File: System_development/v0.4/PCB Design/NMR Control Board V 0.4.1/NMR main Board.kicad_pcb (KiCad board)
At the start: 2 copper layers, 139.7 x 88.9 mm, 58 parts

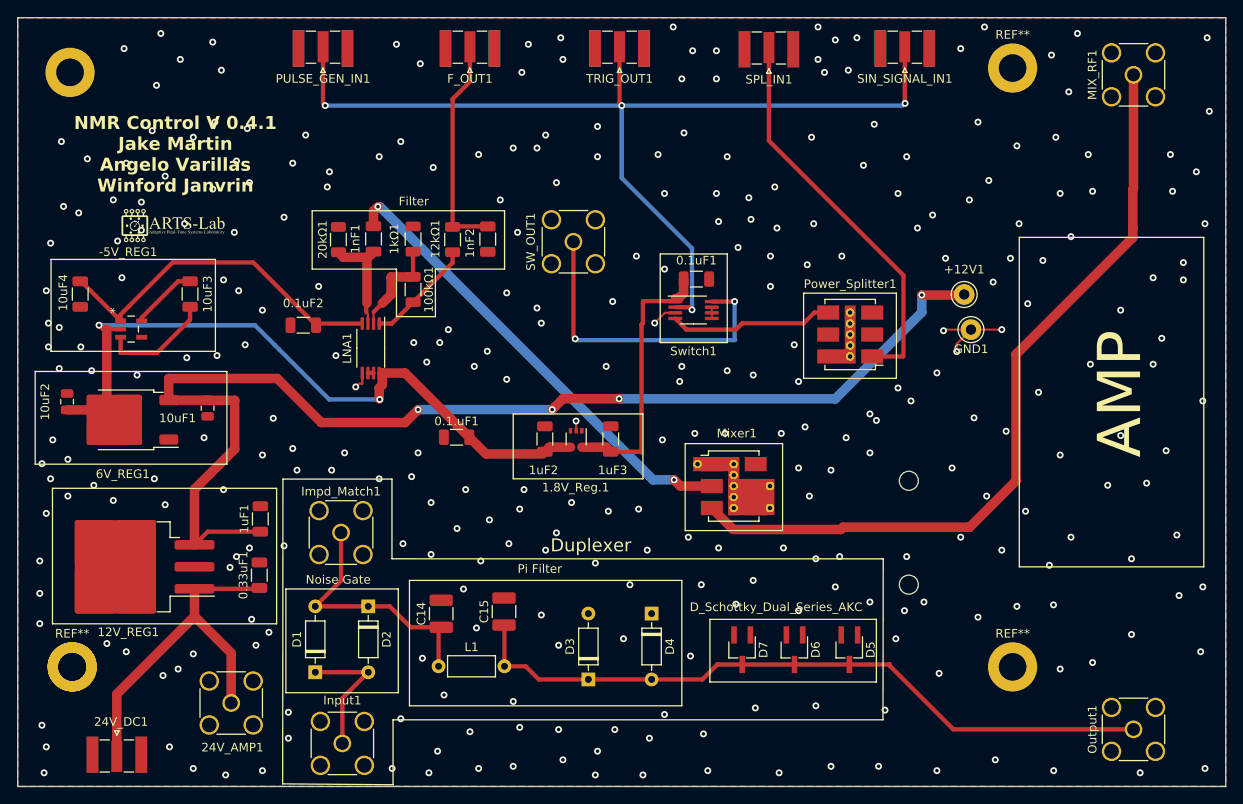
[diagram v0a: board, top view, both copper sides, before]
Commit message: Updated the NMR Board
No warning on the board, looks good order
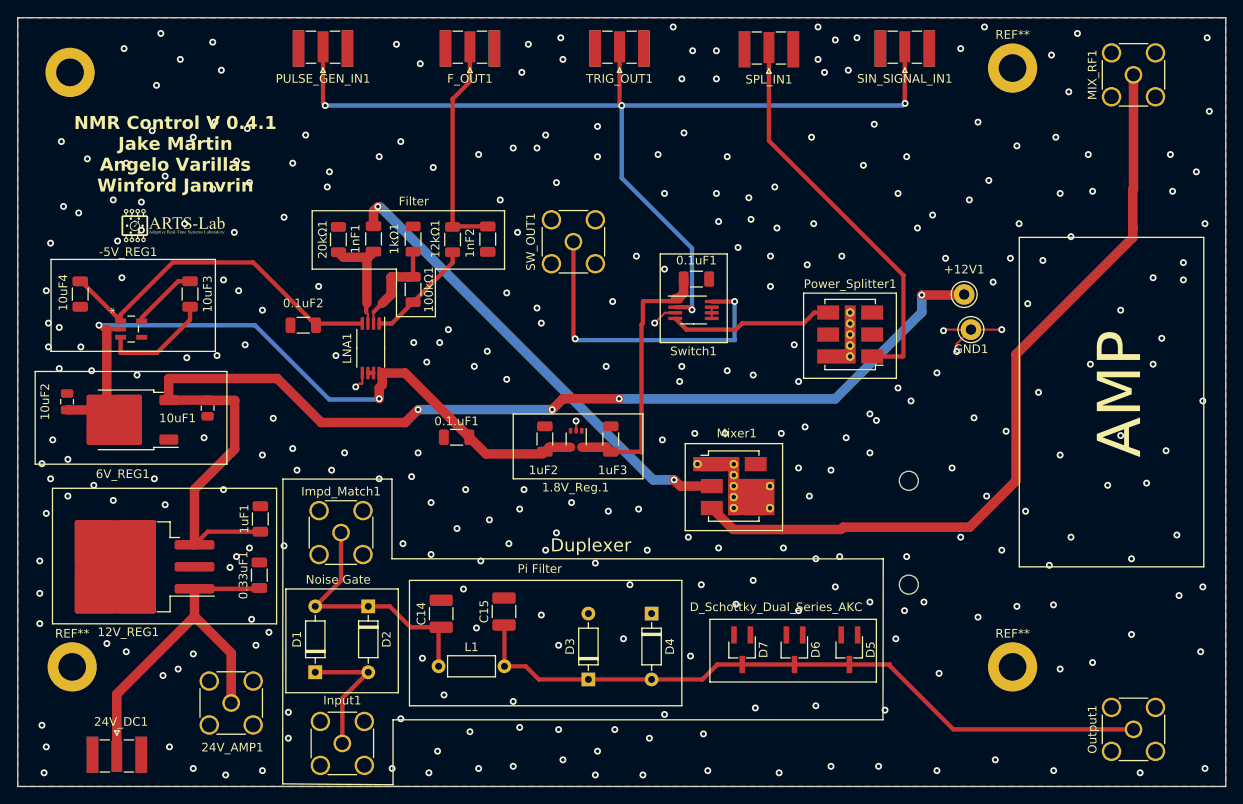
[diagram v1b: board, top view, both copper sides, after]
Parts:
- removed the REF** at (82.5, 118.2)
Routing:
- net Net-(D3-K): track 82.7 -> 82.1 mm
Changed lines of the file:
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@@
       (net 25 "Net-(-5V_REG1-C1+)") (pinfunction "C1+") (pintype "passive"))
   )
-  (footprint "MountingHole:MountingHole_3.2mm_M3_ISO7380_Pad" (layer "F.Cu")
-    (at 82.5 118.25)
-    (descr "Mounting Hole 3.2mm, M3, ISO7380")
-    (tags "mounting hole 3.2mm m3 iso7380")
-    (attr exclude_from_pos_files exclude_from_bom)
-    (fp_text reference "REF**" (at 0 -3.85) (layer "F.SilkS") hide
-        (effects (font (size 1 1) (thickness 0.15)))
-    )
-    (fp_text value "MountingHole_3.2mm_M3_ISO7380_Pad" (at 0 3.85) (layer "F.Fab")
-        (effects (font (size 1 1) (thickness 0.15)))
-    )
-    (fp_text user "${REFERENCE}" (at 0 0) (layer "F.Fab")
-        (effects (font (size 1 1) (thickness 0.15)))
-    )
-    (fp_circle (center 0 0) (end 2.85 0)
-      (stroke (width 0.15) (type solid)) (fill none) (layer "Cmts.User"))
-    (fp_circle (center 0 0) (end 3.1 0)
-      (stroke (width 0.05) (type solid)) (fill none) (layer "F.CrtYd"))
-    (pad "3" thru_hole circle (at 0 0) (size 5.7 5.7) (drill 3.2) (layers "*.Cu" "*.Mask"))
-  )
   (footprint "Connector_Coaxial:SMA_Samtec_SMA-J-P-X-ST-EM1_EdgeMount" (layer "F.Cu")
     (at 87.661 128.409)
@@
   (segment (start 159.9844 117.974) (end 166.0296 117.974) (width 0.5) (layer "F.Cu") (net 4))
   (segment (start 149.5044 119.7046) (end 155.3774 119.7046) (width 0.5) (layer "F.Cu") (net 4))
-  (segment (start 172.3644 118.3166) (end 172.3644 117.6531) (width 0.25) (layer "F.Cu") (net 4))
   (segment (start 132.4864 113.4626) (end 132.4864 118.1806) (width 0.5) (layer "F.Cu") (net 4))
   (segment (start 132.4356 113.4118) (end 132.4864 113.4626) (width 0.25) (layer "F.Cu") (net 4))
@@
   (segment (start 104.255 102.616) (end 98.165 102.616) (width 0.5) (layer "F.Cu") (net 13))
   (segment (start 93.666 84.896) (end 106.2066 84.896) (width 1.1) (layer "F.Cu") (net 13))
-  (segment (start 122.5 88.5) (end 122.5444 88.5444) (width 0.5) (layer "F.Cu") (net 13))
   (segment (start 96.641 104.14) (end 96.641 97.7198) (width 1.1) (layer "F.Cu") (net 13))
   (segment (start 122.4556 88.5444) (end 122.5 88.5) (width 0.5) (layer "F.Cu") (net 13))
-  (segment (start 122.5444 88.5444) (end 122.6058 88.5444) (width 0.5) (layer "F.Cu") (net 13))
   (segment (start 121 90) (end 122.4556 88.5444) (width 1.1) (layer "F.Cu") (net 13))
   (segment (start 139.25 87.25) (end 145.75 87.25) (width 1.1) (layer "F.Cu") (net 13))
@@
   (segment (start 87.661 121.3887) (end 87.661 128.609) (width 1.1) (layer "F.Cu") (net 21))
   (segment (start 104.042 109.22) (end 104.14 109.122) (width 0.5) (layer "F.Cu") (net 21))
-  (segment (start 94.1324 71.4756) (end 89.1032 76.5048) (width 0.5) (layer "F.Cu") (net 22))
+  (segment (start 88.1006 77.5074) (end 94.1324 71.4756) (width 0.5) (layer "F.Cu") (net 22))
   (segment (start 88.1006 78.232) (end 83.5286 73.66) (width 0.5) (layer "F.Cu") (net 22))
-  (segment (start 88.1006 77.5074) (end 89.1032 76.5048) (width 0.5) (layer "F.Cu") (net 22))
   (segment (start 110.695 78.74) (end 103.4306 71.4756) (width 0.5) (layer "F.Cu") (net 22))
   (segment (start 110.8895 78.5455) (end 115.998 78.5455) (width 0.5) (layer "F.Cu") (net 22))
@@
   (segment (start 87.1387 88.157) (end 87.366 88.157) (width 0.25) (layer "F.Cu") (net 23))
   (segment (start 89.041 88.157) (end 87.366 88.157) (width 0.25) (layer "F.Cu") (net 23))
+  (segment (start 118 86) (end 118 87.25) (width 1.1) (layer "F.Cu") (net 23))
   (segment (start 121.0007 84.2705) (end 128.4242 91.694) (width 1.1) (layer "F.Cu") (net 23))
   (segment (start 87.366 88.157) (end 87.366 89.682) (width 0.25) (layer "F.Cu") (net 23))
-  (segment (start 118 87.266) (end 118 86) (width 1.1) (layer "F.Cu") (net 23))
   (segment (start 137.6885 92.8455) (end 137.16 93.374) (width 1.1) (layer "F.Cu") (net 23))
   (segment (start 88.1006 79.1845) (end 86.5 79.1845) (width 0.5) (layer "F.Cu") (net 23))
@@
   (segment (start 87.516 89.682) (end 89.041 91.207) (width 0.25) (layer "F.Cu") (net 23))
   (segment (start 86.5 79.1845) (end 86.0425 79.1845) (width 0.5) (layer "F.Cu") (net 23))
-  (segment (start 118.0592 87.3252) (end 118 87.266) (width 0.25) (layer "F.Cu") (net 23))
   (segment (start 85.313 88.535) (end 81.909 88.535) (width 1.1) (layer "F.Cu") (net 23))
-  (segment (start 117.998 87.264) (end 118.0592 87.3252) (width 0.25) (layer "F.Cu") (net 23))
   (segment (start 118.348 85.652) (end 118.348 84.2705) (width 1.1) (layer "F.Cu") (net 23))
   (segment (start 118 86) (end 118.348 85.652) (width 1.1) (layer "F.Cu") (net 23))
-  (via (at 118.0592 87.3252) (size 0.8) (drill 0.4) (layers "F.Cu" "B.Cu") (net 23))
+  (via (at 118 87.25) (size 0.8) (drill 0.4) (layers "F.Cu" "B.Cu") (net 23))
   (via (at 85.598 78.74) (size 0.8) (drill 0.4) (layers "F.Cu" "B.Cu") (net 23))
-  (segment (start 103.632 78.74) (end 105.918 81.026) (width 0.5) (layer "B.Cu") (net 23))
-  (segment (start 118.0592 87.3252) (end 118.11 87.3252) (width 0.5) (layer "B.Cu") (net 23))
-  (segment (start 112.2172 87.3252) (end 118.0592 87.3252) (width 0.5) (layer "B.Cu") (net 23))
-  (segment (start 105.918 81.026) (end 106.426 81.534) (width 0.5) (layer "B.Cu") (net 23))
+  (segment (start 103.632 78.74) (end 112.2172 87.3252) (width 0.5) (layer "B.Cu") (net 23))
   (segment (start 85.598 78.74) (end 103.632 78.74) (width 0.5) (layer "B.Cu") (net 23))
-  (segment (start 106.426 81.534) (end 112.2172 87.3252) (width 0.5) (layer "B.Cu") (net 23))
+  (segment (start 112.2172 87.3252) (end 118.0592 87.3252) (width 0.5) (layer "B.Cu") (net 23))
   (segment (start 96.127 78.117) (end 96.127 76.61) (width 0.5) (layer "F.Cu") (net 24))
   (segment (start 88.1006 81.927) (end 88.0872 81.9404) (width 0.25) (layer "F.Cu") (net 24))
@@
   (via (at 117.856 65.024) (size 0.8) (drill 0.4) (layers "F.Cu" "B.Cu") (net 26))
   (via (at 152.1072 96.6214) (size 0.8) (drill 0.4) (layers "F.Cu" "B.Cu") (net 26))
-  (segment (start 121.6058 68.5531) (end 118.0767 65.024) (width 1.1) (layer "B.Cu") (net 26))
   (segment (start 117.856 65.024) (end 117.856 64.8033) (width 0.25) (layer "B.Cu") (net 26))
   (segment (start 118.0767 65.024) (end 117.856 65.024) (width 0.25) (layer "B.Cu") (net 26))
-  (segment (start 149.6741 96.6214) (end 121.6058 68.5531) (width 1.1) (layer "B.Cu") (net 26))
+  (segment (start 118.0767 65.024) (end 149.6741 96.6214) (width 1.1) (layer "B.Cu") (net 26))
   (segment (start 152.1072 96.6214) (end 149.6741 96.6214) (width 1.1) (layer "B.Cu") (net 26))
   (segment (start 117.856 64.8033) (end 117.96635 64.91365) (width 0.25) (layer "B.Cu") (net 26))
